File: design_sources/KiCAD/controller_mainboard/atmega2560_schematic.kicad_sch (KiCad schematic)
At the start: 16 parts, among them J4 02x03_pinheader, SW2 SW_TACT, U1 ATmega2560-16A, Y3 16MHz

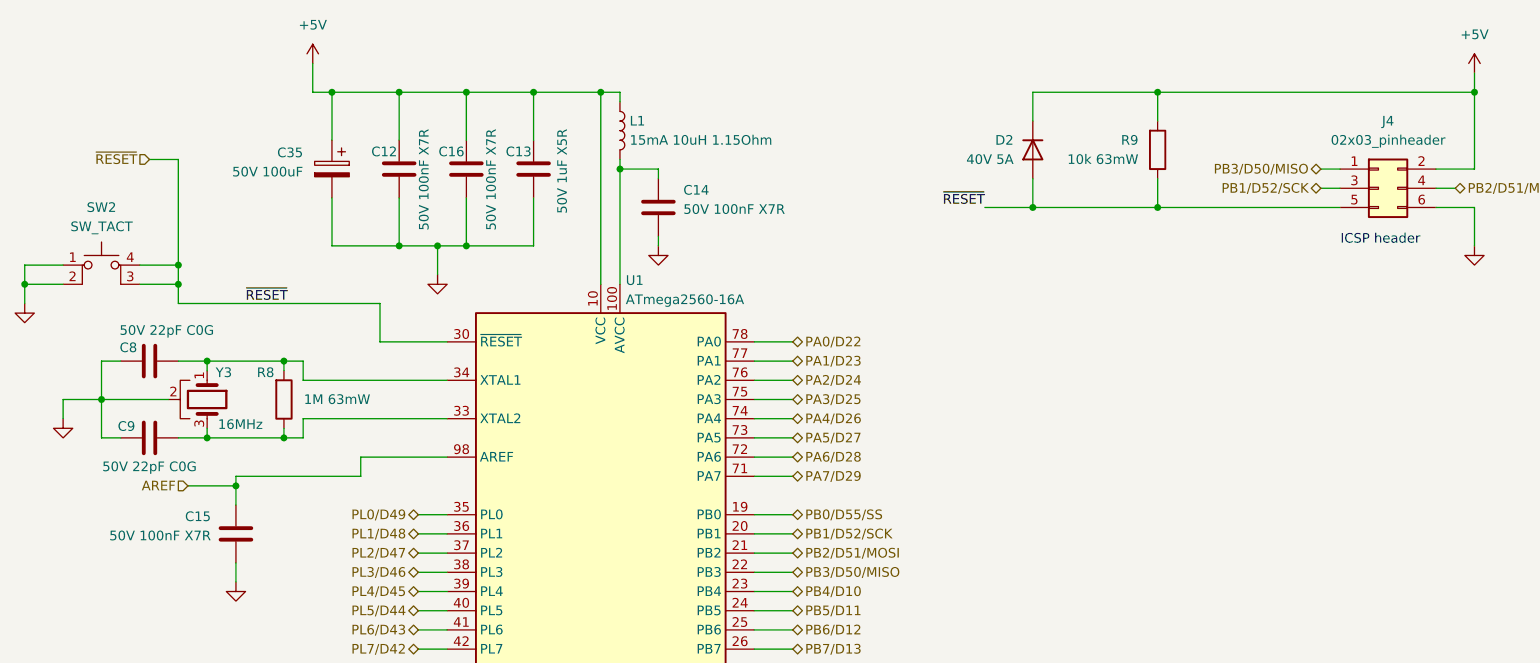
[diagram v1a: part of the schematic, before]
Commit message: Added ESD protection ic, added footprints to all IC and loaded into pcbnew to size up the pcb size.
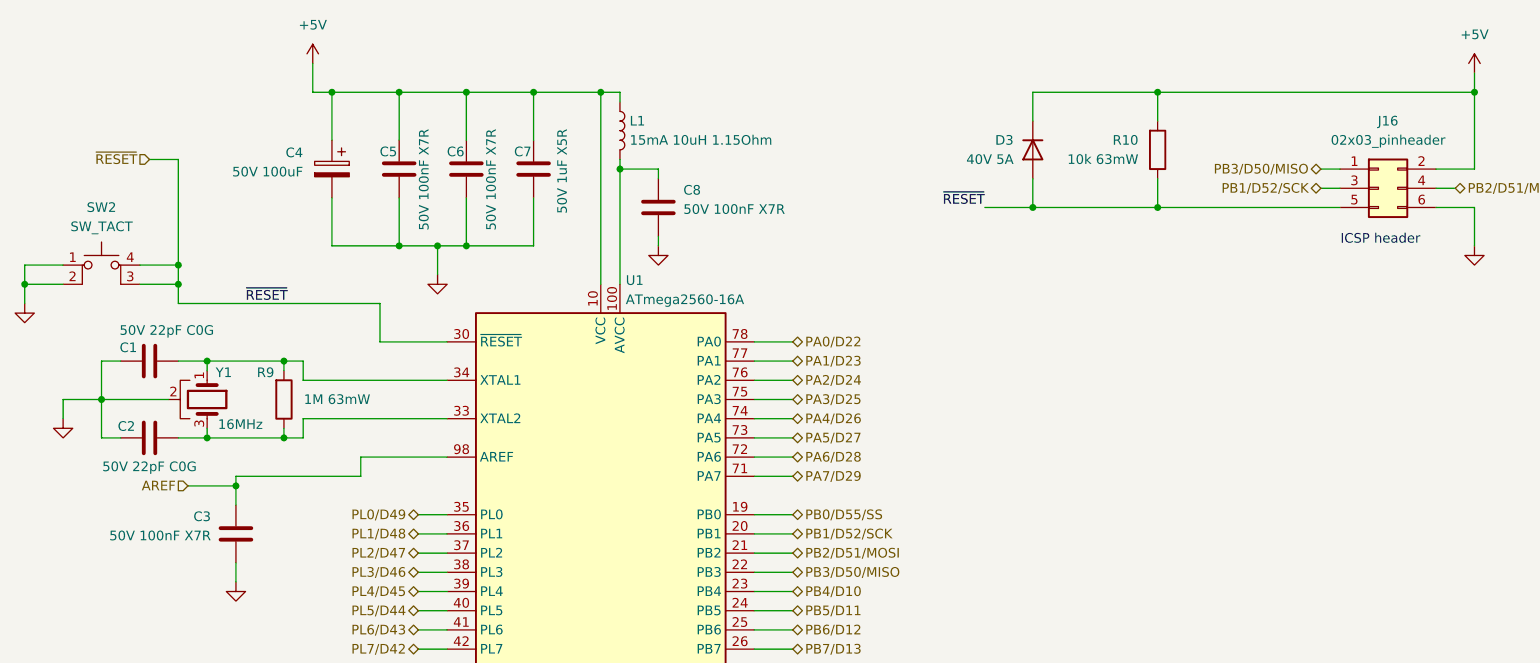
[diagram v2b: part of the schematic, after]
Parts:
- renumbered C8 to C1, C9 to C2, C15 to C3, C35 to C4, C12 to C5, C16 to C6, C13 to C7, C14 to C8, D2 to D3, J4 to J16, R9 to R10, R8 to R9, Y3 to Y1
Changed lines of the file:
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@@
 		(dnp no)
 		(fields_autoplaced yes)
-		(property "Reference" "#PWR017"
+		(property "Reference" "#PWR051"
 			(at 290.83 58.42 0)
 			(effects
@@
 			(project "controller_mainboard"
 				(path "/0fdfffec-3d24-4249-8ba9-dae7a6ccc250/104cadd7-dded-4cf0-b82f-f956a8bd9cde"
-					(reference "#PWR017")
+					(reference "#PWR051")
 					(unit 1)
 				)
@@
 		(on_board yes)
 		(dnp no)
-		(property "Reference" "C14"
+		(property "Reference" "C8"
 			(at 186.182 44.704 0)
 			(effects
@@
 			(project "controller_mainboard"
 				(path "/0fdfffec-3d24-4249-8ba9-dae7a6ccc250/104cadd7-dded-4cf0-b82f-f956a8bd9cde"
-					(reference "C14")
+					(reference "C8")
 					(unit 1)
 				)
@@
 		(on_board yes)
 		(dnp no)
-		(property "Reference" "C13"
+		(property "Reference" "C7"
 			(at 166.116 39.624 0)
 			(effects
@@
 			(project "controller_mainboard"
 				(path "/0fdfffec-3d24-4249-8ba9-dae7a6ccc250/104cadd7-dded-4cf0-b82f-f956a8bd9cde"
-					(reference "C13")
+					(reference "C7")
 					(unit 1)
 				)
@@
 		(on_board yes)
 		(dnp no)
-		(property "Reference" "R9"
+		(property "Reference" "R10"
 			(at 246.38 38.0999 0)
 			(effects
@@
 			(project "controller_mainboard"
 				(path "/0fdfffec-3d24-4249-8ba9-dae7a6ccc250/104cadd7-dded-4cf0-b82f-f956a8bd9cde"
-					(reference "R9")
+					(reference "R10")
 					(unit 1)
 				)
@@
 		(on_board yes)
 		(dnp no)
-		(property "Reference" "C16"
+		(property "Reference" "C6"
 			(at 157.226 39.624 0)
 			(effects
@@
 			(project "controller_mainboard"
 				(path "/0fdfffec-3d24-4249-8ba9-dae7a6ccc250/104cadd7-dded-4cf0-b82f-f956a8bd9cde"
-					(reference "C16")
+					(reference "C6")
 					(unit 1)
 				)
@@
 		(on_board yes)
 		(dnp no)
-		(property "Reference" "R8"
+		(property "Reference" "R9"
 			(at 132.08 68.834 0)
 			(effects
@@
 			(project "controller_mainboard"
 				(path "/0fdfffec-3d24-4249-8ba9-dae7a6ccc250/104cadd7-dded-4cf0-b82f-f956a8bd9cde"
-					(reference "R8")
+					(reference "R9")
 					(unit 1)
 				)
@@
 		(on_board yes)
 		(dnp no)
-		(property "Reference" "C9"
+		(property "Reference" "C2"
 			(at 112.522 75.946 90)
 			(effects
@@
 			(project "controller_mainboard"
 				(path "/0fdfffec-3d24-4249-8ba9-dae7a6ccc250/104cadd7-dded-4cf0-b82f-f956a8bd9cde"
-					(reference "C9")
+					(reference "C2")
 					(unit 1)
 				)
@@
 		(dnp no)
 		(fields_autoplaced yes)
-		(property "Reference" "#PWR014"
+		(property "Reference" "#PWR049"
 			(at 182.88 58.42 0)
 			(effects
@@
 			(project "controller_mainboard"
 				(path "/0fdfffec-3d24-4249-8ba9-dae7a6ccc250/104cadd7-dded-4cf0-b82f-f956a8bd9cde"
-					(reference "#PWR014")
+					(reference "#PWR049")
 					(unit 1)
 				)
@@
 		(on_board yes)
 		(dnp no)
-		(property "Reference" "C12"
+		(property "Reference" "C5"
 			(at 148.336 39.624 0)
 			(effects
@@
 			(project "controller_mainboard"
 				(path "/0fdfffec-3d24-4249-8ba9-dae7a6ccc250/104cadd7-dded-4cf0-b82f-f956a8bd9cde"
-					(reference "C12")
+					(reference "C5")
 					(unit 1)
 				)
@@
 		(on_board yes)
 		(dnp no)
-		(property "Reference" "C15"
+		(property "Reference" "C3"
 			(at 123.698 87.884 0)
 			(effects
@@
 			(project "controller_mainboard"
 				(path "/0fdfffec-3d24-4249-8ba9-dae7a6ccc250/104cadd7-dded-4cf0-b82f-f956a8bd9cde"
-					(reference "C15")
+					(reference "C3")
 					(unit 1)
 				)
@@
 		(dnp no)
 		(fields_autoplaced yes)
-		(property "Reference" "#PWR010"
+		(property "Reference" "#PWR044"
 			(at 104.14 81.28 0)
 			(effects
@@
 			(project "controller_mainboard"
 				(path "/0fdfffec-3d24-4249-8ba9-dae7a6ccc250/104cadd7-dded-4cf0-b82f-f956a8bd9cde"
-					(reference "#PWR010")
+					(reference "#PWR044")
 					(unit 1)
 				)
@@
 		(dnp no)
 		(fields_autoplaced yes)
-		(property "Reference" "J4"
+		(property "Reference" "J16"
 			(at 279.4 35.56 0)
 			(effects
@@
 			(project "controller_mainboard"
 				(path "/0fdfffec-3d24-4249-8ba9-dae7a6ccc250/104cadd7-dded-4cf0-b82f-f956a8bd9cde"
-					(reference "J4")
+					(reference "J16")
 					(unit 1)
 				)
@@
 		(on_board yes)
 		(dnp no)
-		(property "Reference" "D2"
+		(property "Reference" "D3"
 			(at 229.87 38.0999 90)
 			(effects
@@
 			(project "controller_mainboard"
 				(path "/0fdfffec-3d24-4249-8ba9-dae7a6ccc250/104cadd7-dded-4cf0-b82f-f956a8bd9cde"
-					(reference "D2")
+					(reference "D3")
 					(unit 1)
 				)
@@
 		(dnp no)
 		(fields_autoplaced yes)
-		(property "Reference" "#PWR012"
+		(property "Reference" "#PWR047"
 			(at 153.67 62.23 0)
 			(effects
@@
 			(project "controller_mainboard"
 				(path "/0fdfffec-3d24-4249-8ba9-dae7a6ccc250/104cadd7-dded-4cf0-b82f-f956a8bd9cde"
-					(reference "#PWR012")
+					(reference "#PWR047")
 					(unit 1)
 				)
@@
 		(on_board yes)
 		(dnp no)
-		(property "Reference" "Y3"
+		(property "Reference" "Y1"
 			(at 126.492 68.834 90)
 			(effects
@@
 			(project "controller_mainboard"
 				(path "/0fdfffec-3d24-4249-8ba9-dae7a6ccc250/104cadd7-dded-4cf0-b82f-f956a8bd9cde"
-					(reference "Y3")
+					(reference "Y1")
 					(unit 1)
 				)
@@
 		(on_board yes)
 		(dnp no)
-		(property "Reference" "C8"
+		(property "Reference" "C1"
 			(at 112.776 65.532 90)
 			(effects
@@
 			(project "controller_mainboard"
 				(path "/0fdfffec-3d24-4249-8ba9-dae7a6ccc250/104cadd7-dded-4cf0-b82f-f956a8bd9cde"
-					(reference "C8")
+					(reference "C1")
 					(unit 1)
 				)
@@
 		(dnp no)
 		(fields_autoplaced yes)
-		(property "Reference" "#PWR011"
+		(property "Reference" "#PWR046"
 			(at 137.16 31.75 0)
 			(effects
@@
 			(project ""
 				(path "/0fdfffec-3d24-4249-8ba9-dae7a6ccc250/104cadd7-dded-4cf0-b82f-f956a8bd9cde"
-					(reference "#PWR011")
+					(reference "#PWR046")
 					(unit 1)
 				)
@@
 		(on_board yes)
 		(dnp no)
-		(property "Reference" "C35"
+		(property "Reference" "C4"
 			(at 135.89 39.7509 0)
 			(effects
@@
 			(project "controller_mainboard"
 				(path "/0fdfffec-3d24-4249-8ba9-dae7a6ccc250/104cadd7-dded-4cf0-b82f-f956a8bd9cde"
-					(reference "C35")
+					(reference "C4")
 					(unit 1)
 				)
@@
 		(dnp no)
 		(fields_autoplaced yes)
-		(property "Reference" "#PWR013"
+		(property "Reference" "#PWR048"
 			(at 175.26 214.63 0)
 			(effects
@@
 			(project "controller_mainboard"
 				(path "/0fdfffec-3d24-4249-8ba9-dae7a6ccc250/104cadd7-dded-4cf0-b82f-f956a8bd9cde"
-					(reference "#PWR013")
+					(reference "#PWR048")
 					(unit 1)
 				)
@@
 		(dnp no)
 		(fields_autoplaced yes)
-		(property "Reference" "#PWR016"
+		(property "Reference" "#PWR050"
 			(at 290.83 33.02 0)
 			(effects
@@
 			(project "controller_mainboard"
 				(path "/0fdfffec-3d24-4249-8ba9-dae7a6ccc250/104cadd7-dded-4cf0-b82f-f956a8bd9cde"
-					(reference "#PWR016")
+					(reference "#PWR050")
 					(unit 1)
 				)
@@
 		(dnp no)
 		(fields_autoplaced yes)
-		(property "Reference" "#PWR015"
+		(property "Reference" "#PWR045"
 			(at 127 102.87 0)
 			(effects
@@
 			(project "controller_mainboard"
 				(path "/0fdfffec-3d24-4249-8ba9-dae7a6ccc250/104cadd7-dded-4cf0-b82f-f956a8bd9cde"
-					(reference "#PWR015")
+					(reference "#PWR045")
 					(unit 1)
 				)
@@
 		(dnp no)
 		(fields_autoplaced yes)
-		(property "Reference" "#PWR021"
+		(property "Reference" "#PWR043"
 			(at 99.06 66.04 0)
 			(effects
@@
 			(project "controller_mainboard"
 				(path "/0fdfffec-3d24-4249-8ba9-dae7a6ccc250/104cadd7-dded-4cf0-b82f-f956a8bd9cde"
-					(reference "#PWR021")
-					(unit 1)
-				)
+					(reference "#PWR043")
+					(unit 1)
+				)

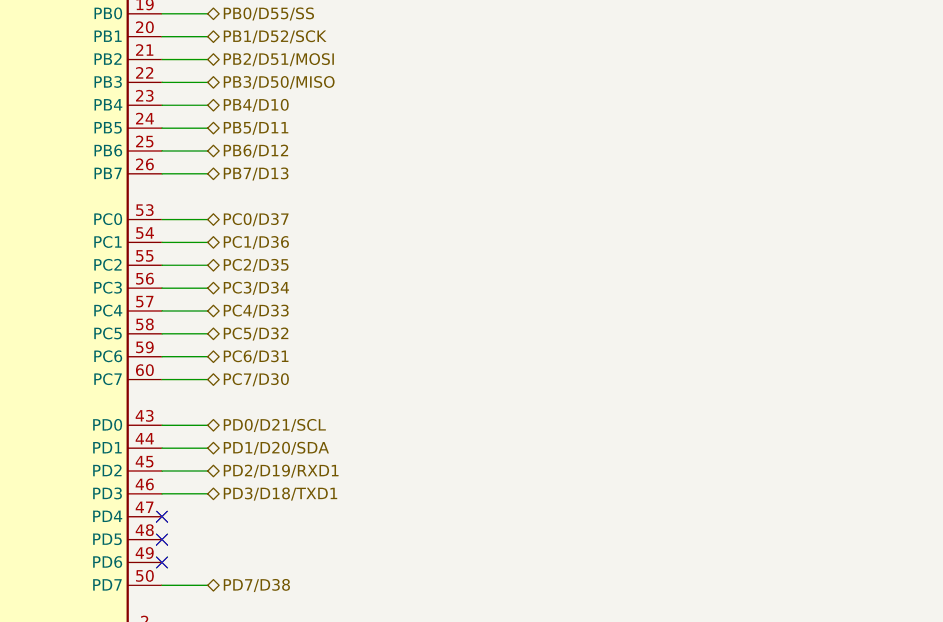
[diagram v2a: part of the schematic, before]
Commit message: Read through schematic to bugfix.
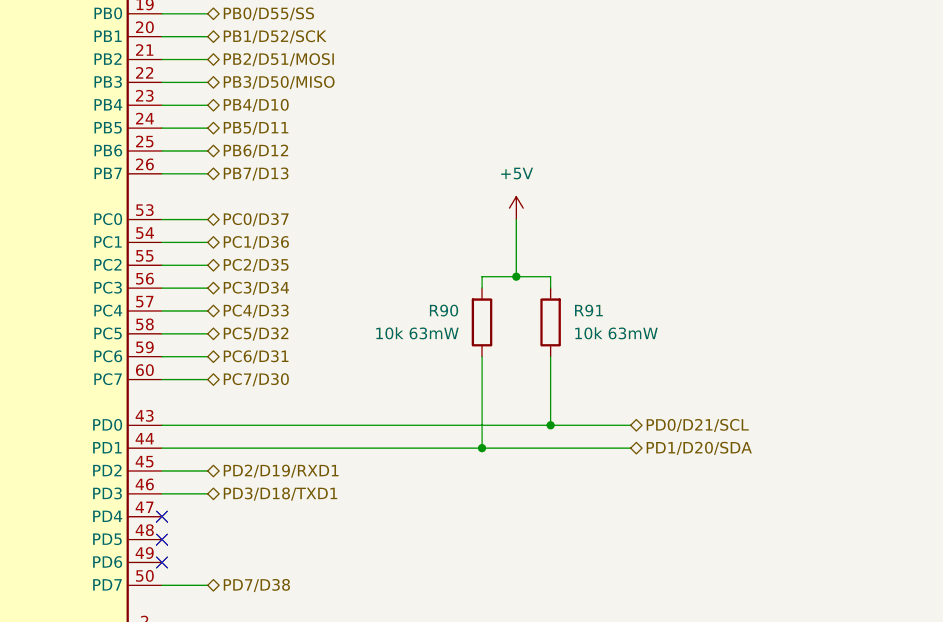
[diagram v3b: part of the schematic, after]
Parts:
- added R90, R91: 10k 63mW, Resistor_SMD:R_0402_1005Metric, symbol Device:R
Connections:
- net +5V: now also R90.2, R91.2
- net PD0/D21/SCL: now also R91.1
- net PD1/D20/SDA: now also R90.1

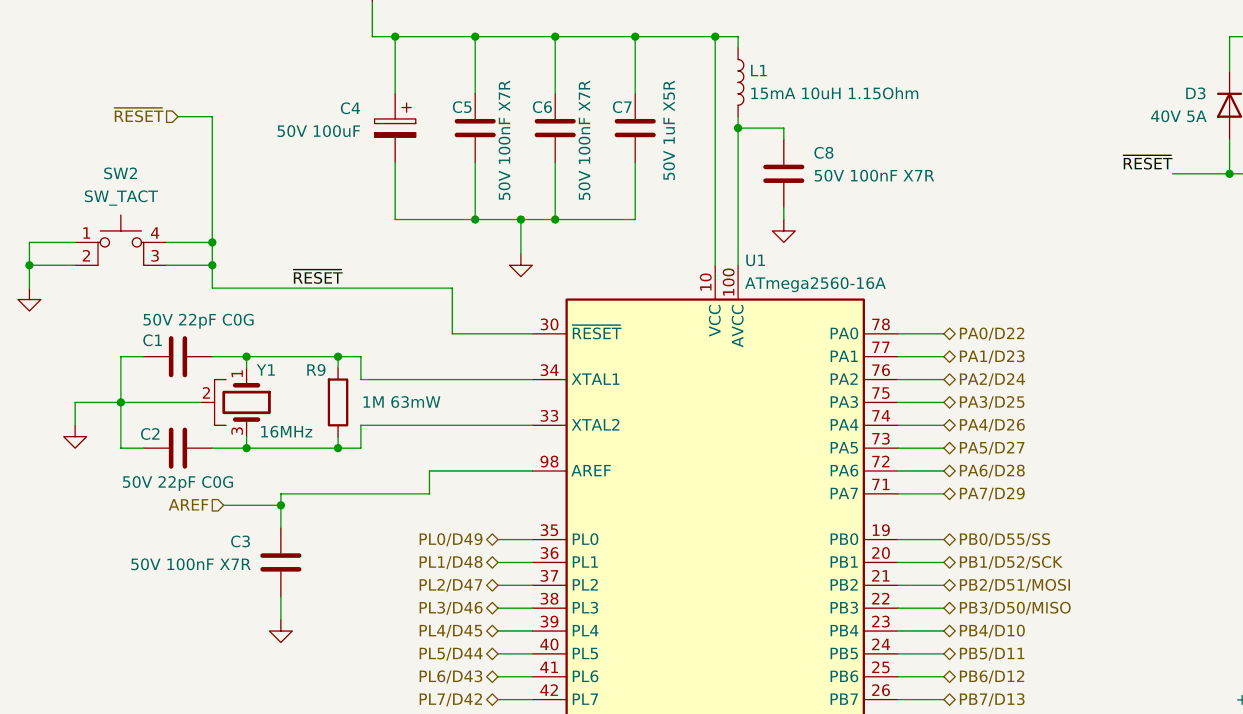
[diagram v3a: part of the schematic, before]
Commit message: Adjusted gitignore to ignore backups, removed backup files
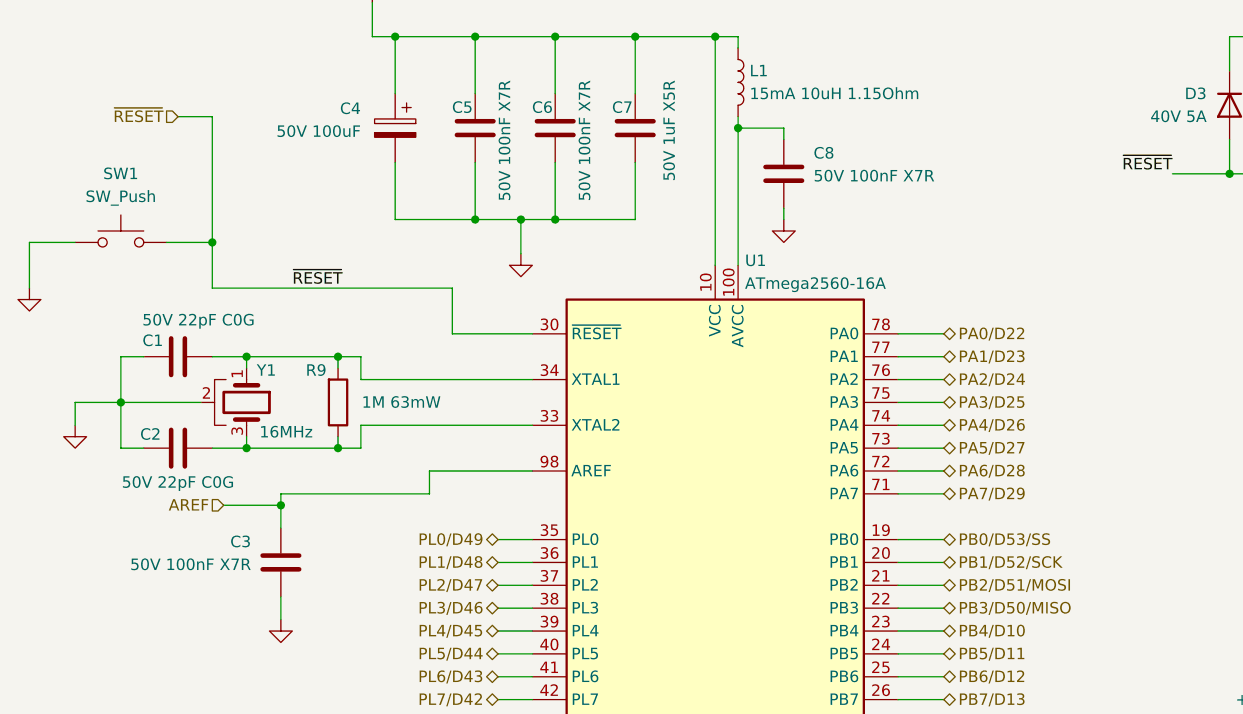
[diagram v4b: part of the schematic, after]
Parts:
- removed SW2: SW_TACT, Button_Switch_SMD:SW_MEC_5GSH9, symbol Switch:SW_MEC_5E
- added SW1: SW_Push, Button_Switch_SMD:SW_SPST_PTS645, symbol Switch:SW_Push
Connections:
- net GND: now also SW1.1
- net ~{RESET}: now also SW1.2
- net PB0/D55/SS renamed PB0/D53/SS
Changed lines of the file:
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@@
 	)
 	(junction
-		(at 99.06 57.15)
-		(diameter 0)
-		(color 0 0 0 0)
-	)
-	(junction
 		(at 232.41 46.99)
 		(diameter 0)
@@
 	)
 	(junction
-		(at 119.38 57.15)
-		(diameter 0)
-		(color 0 0 0 0)
-	)
-	(junction
 		(at 133.35 67.31)
 		(diameter 0)
@@
 	(wire
 		(pts
-			(xy 99.06 57.15) (xy 99.06 59.69)
+			(xy 99.06 54.61) (xy 99.06 59.69)
 		)
 		(stroke
@@
 	(wire
 		(pts
-			(xy 104.14 57.15) (xy 99.06 57.15)
-		)
-		(stroke
-			(width 0)
-			(type default)
-		)
-	)
-	(wire
-		(pts
 			(xy 148.59 31.75) (xy 148.59 38.1)
 		)
@@
 	(wire
 		(pts
-			(xy 119.38 57.15) (xy 114.3 57.15)
-		)
-		(stroke
-			(width 0)
-			(type default)
-		)
-	)
-	(wire
-		(pts
 			(xy 151.13 181.61) (xy 154.94 181.61)
 		)
@@
 	(wire
 		(pts
-			(xy 119.38 59.69) (xy 119.38 57.15)
-		)
-		(stroke
-			(width 0)
-			(type default)
-		)
-	)
-	(wire
-		(pts
 			(xy 200.66 92.71) (xy 195.58 92.71)
 		)
@@
 	(wire
 		(pts
-			(xy 99.06 54.61) (xy 99.06 57.15)
-		)
-		(stroke
-			(width 0)
-			(type default)
-		)
-	)
-	(wire
-		(pts
 			(xy 153.67 52.07) (xy 153.67 55.88)
 		)
@@
 	(wire
 		(pts
-			(xy 119.38 57.15) (xy 119.38 54.61)
+			(xy 119.38 54.61) (xy 119.38 59.69)
 		)
 		(stroke
@@
 		)
 	)
-	(hierarchical_label "PB0{slash}D55{slash}SS"
+	(hierarchical_label "PB0{slash}D53{slash}SS"
 		(shape bidirectional)
 		(at 200.66 87.63 0)
@@
 	)
 	(symbol
+		(lib_id "Switch:SW_Push")
+		(at 109.22 54.61 0)
+		(unit 1)
+		(exclude_from_sim no)
+		(in_bom yes)
+		(on_board yes)
+		(dnp no)
+		(fields_autoplaced yes)
+		(property "Reference" "SW1"
+			(at 109.22 46.99 0)
+			(effects
+				(font
+					(size 1.27 1.27)
+				)
+			)
+		)
+		(property "Value" "SW_Push"
+			(at 109.22 49.53 0)
+			(effects
+				(font
+					(size 1.27 1.27)
+				)
+			)
+		)
+		(property "Footprint" "Button_Switch_SMD:SW_SPST_PTS645"
+			(at 109.22 49.53 0)
+			(effects
+				(font
+					(size 1.27 1.27)
+				)
+				(hide yes)
+			)
+		)
+		(property "Datasheet" "~"
+			(at 109.22 49.53 0)
+			(effects
+				(font
+					(size 1.27 1.27)
+				)
+				(hide yes)
+			)
+		)
+		(property "Description" "Push button switch, generic, two pins"
+			(at 109.22 54.61 0)
+			(effects
+				(font
+					(size 1.27 1.27)
+				)
+				(hide yes)
+			)
+		)
+		(property "JLCPCB" "C19191552"
+			(at 109.22 54.61 0)
+			(effects
+				(font
+					(size 1.27 1.27)
+				)
+				(hide yes)
+			)
+		)
+		(pin "2"
+		)
+		(pin "1"
+		)
+		(instances
+			(project ""
+				(path "/0fdfffec-3d24-4249-8ba9-dae7a6ccc250/104cadd7-dded-4cf0-b82f-f956a8bd9cde"
+					(reference "SW1")
+					(unit 1)
+				)
+			)
+		)
+	)
+	(symbol
 		(lib_id "Device:R")
 		(at 133.35 72.39 0)
@@
 					(unit 1)
 				)
-			)
-		)
-	)
-	(symbol
-		(lib_id "Switch:SW_MEC_5E")
-		(at 109.22 57.15 0)
-		(unit 1)
-		(exclude_from_sim no)
-		(in_bom yes)
-		(on_board yes)
-		(dnp no)
-		(fields_autoplaced yes)
-		(property "Reference" "SW2"
-			(at 109.22 46.99 0)
-			(effects
-				(font
-					(size 1.27 1.27)
-				)
-			)
-		)
-		(property "Value" "SW_TACT"
-			(at 109.22 49.53 0)
-			(effects
-				(font
-					(size 1.27 1.27)
-				)
-			)
-		)
-		(property "Footprint" "Button_Switch_SMD:SW_MEC_5GSH9"
-			(at 109.22 49.53 0)
-			(effects
-				(font
-					(size 1.27 1.27)
-				)
-				(hide yes)
-			)
-		)
-		(property "Datasheet" "http://www.apem.com/int/index.php?controller=attachment&id_attachment=1371"
-			(at 109.22 49.53 0)
-			(effects
-				(font
-					(size 1.27 1.27)
-				)
-				(hide yes)
-			)
-		)
-		(property "Description" "MEC 5E single pole normally-open tactile switch"
-			(at 109.22 57.15 0)
-			(effects
-				(font
-					(size 1.27 1.27)
-				)
-				(hide yes)
-			)
-		)
-		(property "JLCPCB" "C19191552"
-			(at 109.22 57.15 0)
-			(effects
-				(font
-					(size 1.27 1.27)
-				)
-				(hide yes)
-			)
-		)
-		(pin "3"
-		)
-		(pin "1"
-		)
-		(pin "4"
-		)
-		(pin "2"
-		)
-		(instances
-			(project ""
-				(path "/0fdfffec-3d24-4249-8ba9-dae7a6ccc250/104cadd7-dded-4cf0-b82f-f956a8bd9cde"
-					(reference "SW2")
-					(unit 1)
-				)
